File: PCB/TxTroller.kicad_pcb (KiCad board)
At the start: 2 copper layers, 19.9 x 34 mm, 8 parts, among them J1 RadioReceiver, Q1 2N2222, U1 XIAO-RP2040-DIP

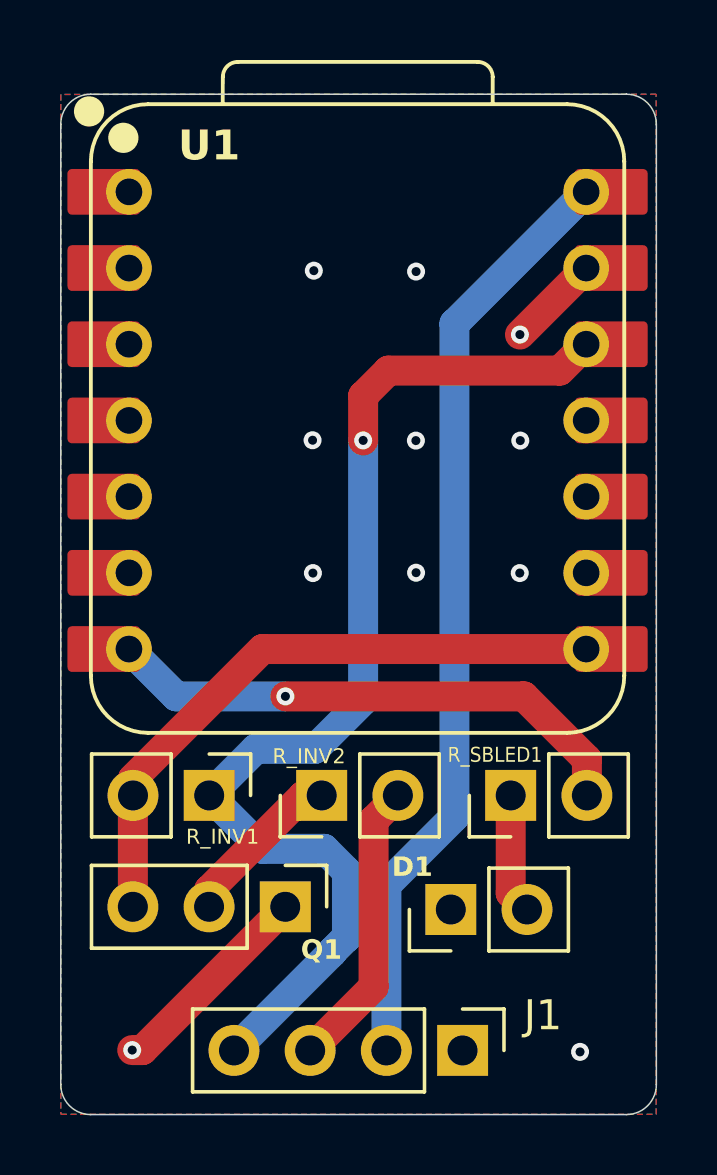
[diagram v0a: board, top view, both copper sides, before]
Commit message: fixed drc errs
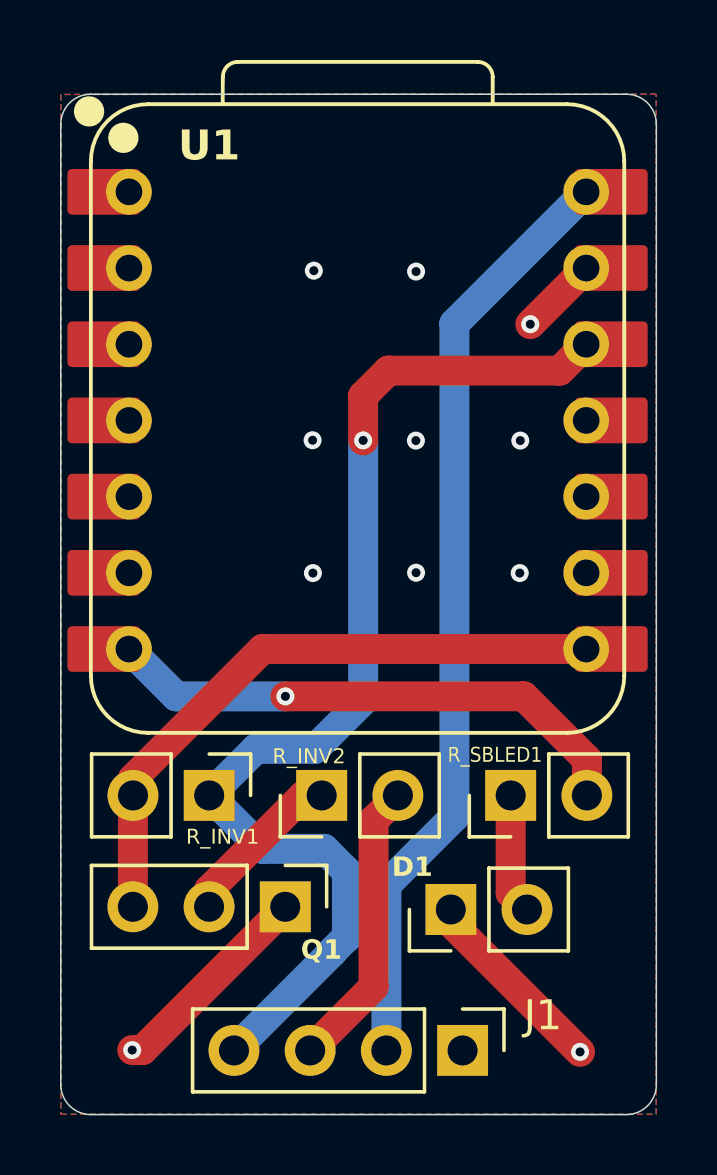
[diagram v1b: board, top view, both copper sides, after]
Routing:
- net GND: track 10.2 -> 16.3 mm
